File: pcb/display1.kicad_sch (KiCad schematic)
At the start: 35 parts, among them Q1 2N7002K, Q10 BSS84, Q11 BSS84, Q12 BSS84, Q2 2N7002K, Q3 2N7002K, Q4 2N7002K, Q5 BSS84, Q6 BSS84, Q7 BSS84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

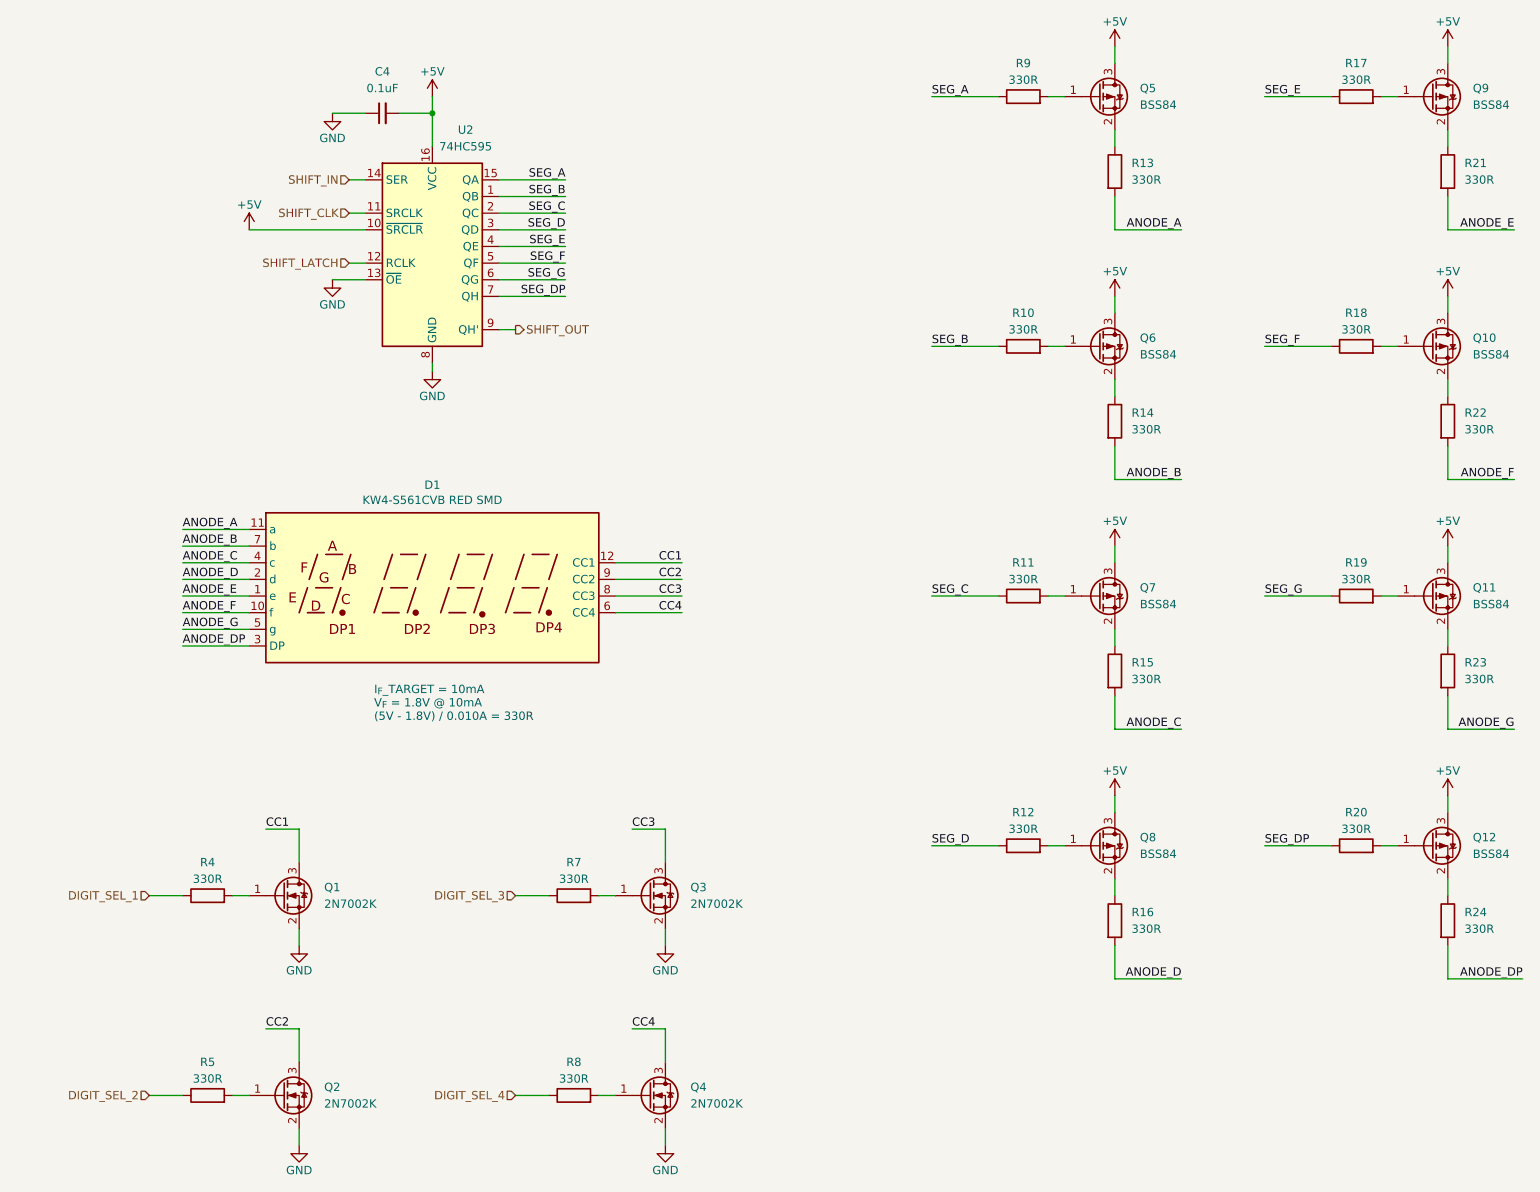
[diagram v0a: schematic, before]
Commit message: tentative schematic for common cathode
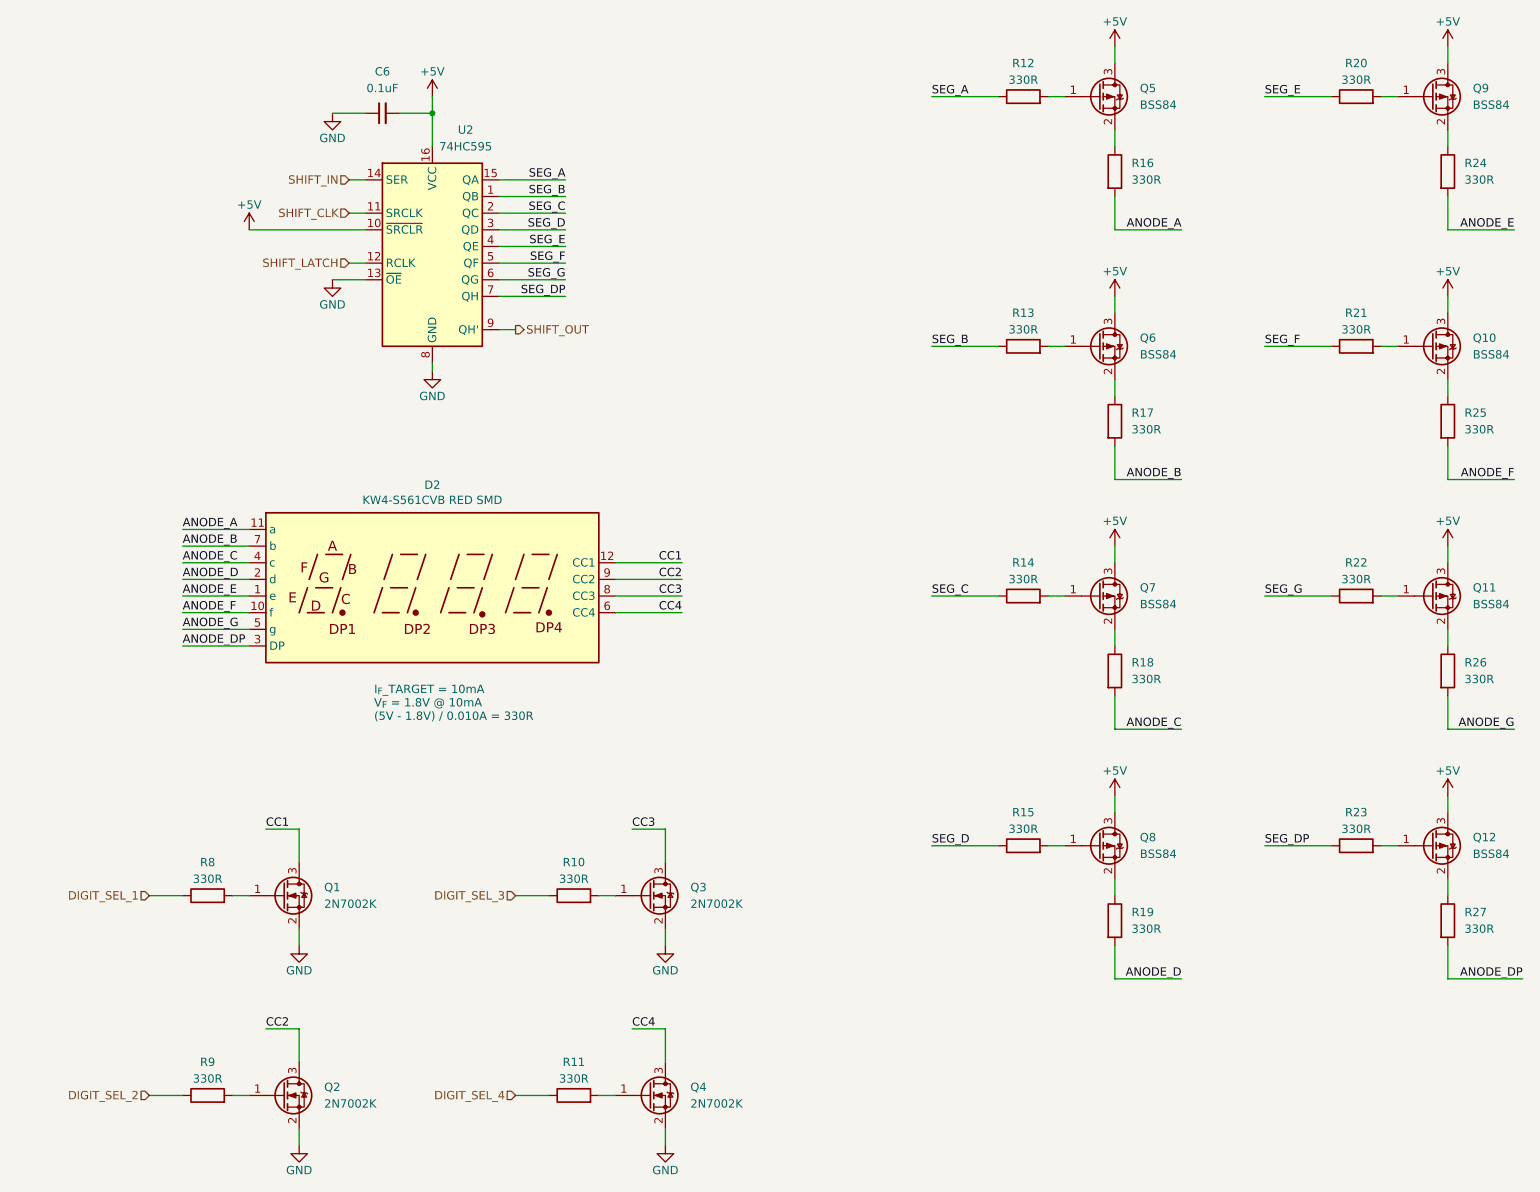
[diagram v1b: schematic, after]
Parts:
- C6: renamed from C4; footprint (none) -> Capacitor_SMD:C_0805_2012Metric_Pad1.18x1.45mm_HandSolder
- R10: renamed from R7; footprint Resistor_SMD:R_0805_2012Metric_Pad1.15x1.40mm_HandSolder -> Resistor_SMD:R_0805_2012Metric_Pad1.20x1.40mm_HandSolder
- R11: renamed from R8; footprint Resistor_SMD:R_0805_2012Metric_Pad1.15x1.40mm_HandSolder -> Resistor_SMD:R_0805_2012Metric_Pad1.20x1.40mm_HandSolder
- R12: renamed from R9; footprint Resistor_SMD:R_0805_2012Metric_Pad1.15x1.40mm_HandSolder -> Resistor_SMD:R_0805_2012Metric_Pad1.20x1.40mm_HandSolder
- R13: renamed from R10; footprint Resistor_SMD:R_0805_2012Metric_Pad1.15x1.40mm_HandSolder -> Resistor_SMD:R_0805_2012Metric_Pad1.20x1.40mm_HandSolder
- R14: renamed from R11; footprint Resistor_SMD:R_0805_2012Metric_Pad1.15x1.40mm_HandSolder -> Resistor_SMD:R_0805_2012Metric_Pad1.20x1.40mm_HandSolder
- R15: renamed from R12; footprint Resistor_SMD:R_0805_2012Metric_Pad1.15x1.40mm_HandSolder -> Resistor_SMD:R_0805_2012Metric_Pad1.20x1.40mm_HandSolder
- R16: renamed from R13; footprint (none) -> Resistor_SMD:R_0805_2012Metric_Pad1.20x1.40mm_HandSolder
- R17: renamed from R14; footprint (none) -> Resistor_SMD:R_0805_2012Metric_Pad1.20x1.40mm_HandSolder
- R18: renamed from R15; footprint (none) -> Resistor_SMD:R_0805_2012Metric_Pad1.20x1.40mm_HandSolder
- R19: renamed from R16; footprint (none) -> Resistor_SMD:R_0805_2012Metric_Pad1.20x1.40mm_HandSolder
- R20: renamed from R17; footprint Resistor_SMD:R_0805_2012Metric_Pad1.15x1.40mm_HandSolder -> Resistor_SMD:R_0805_2012Metric_Pad1.20x1.40mm_HandSolder
- R21: renamed from R18; footprint Resistor_SMD:R_0805_2012Metric_Pad1.15x1.40mm_HandSolder -> Resistor_SMD:R_0805_2012Metric_Pad1.20x1.40mm_HandSolder
- R22: renamed from R19; footprint Resistor_SMD:R_0805_2012Metric_Pad1.15x1.40mm_HandSolder -> Resistor_SMD:R_0805_2012Metric_Pad1.20x1.40mm_HandSolder
- R23: renamed from R20; footprint Resistor_SMD:R_0805_2012Metric_Pad1.15x1.40mm_HandSolder -> Resistor_SMD:R_0805_2012Metric_Pad1.20x1.40mm_HandSolder
- R24: renamed from R21; footprint (none) -> Resistor_SMD:R_0805_2012Metric_Pad1.20x1.40mm_HandSolder
- R25: renamed from R22; footprint (none) -> Resistor_SMD:R_0805_2012Metric_Pad1.20x1.40mm_HandSolder
- R26: renamed from R23; footprint (none) -> Resistor_SMD:R_0805_2012Metric_Pad1.20x1.40mm_HandSolder
- R27: renamed from R24; footprint (none) -> Resistor_SMD:R_0805_2012Metric_Pad1.20x1.40mm_HandSolder
- R8: renamed from R4; footprint Resistor_SMD:R_0805_2012Metric_Pad1.15x1.40mm_HandSolder -> Resistor_SMD:R_0805_2012Metric_Pad1.20x1.40mm_HandSolder
- R9: renamed from R5; footprint Resistor_SMD:R_0805_2012Metric_Pad1.15x1.40mm_HandSolder -> Resistor_SMD:R_0805_2012Metric_Pad1.20x1.40mm_HandSolder
- renumbered D1 to D2

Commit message: common anode schematic
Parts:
- removed C6: 0.1uF, Capacitor_SMD:C_0805_2012Metric_Pad1.18x1.45mm_HandSolder, symbol Device:C_Small
- removed D2: KW4-S561CVB RED SMD, mtg_life_counter:KW4-S561xxB_SMD, symbol mtg_life_counter:KW4-S561CxB
- removed Q1, Q2, Q3, Q4: 2N7002K, Package_TO_SOT_SMD:SOT-23, symbol Transistor_FET:2N7002K
- removed Q10, Q11, Q12, Q5, Q6, Q7, Q8, Q9: BSS84, Package_TO_SOT_SMD:SOT-23, symbol Transistor_FET:BSS84
- removed R21, R22, R23, R24, R25, R26, R27: 330R, Resistor_SMD:R_0805_2012Metric_Pad1.20x1.40mm_HandSolder, symbol Device:R
- removed U2: 74HC595, Package_SO:SOIC-16_3.9x9.9mm_P1.27mm, symbol 74xx:74HC595
- added D2: KW4-S561AVB, mtg_life_counter:KW4-S561xxB_SMD, symbol mtg_life_counter:KW4-S561AxB
- added Q1, Q2, Q3, Q4: DMG2301L, Package_TO_SOT_SMD:SOT-23, symbol Transistor_FET:DMG2301L
- added U2: TPIC6C596, Package_SO:SOIC-16_3.9x9.9mm_P1.27mm, symbol mtg_life_counter:TPIC6C596
- R20: value 330R -> 10k
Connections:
- net SEG_E is gone; now on net +5V: R20.1
- net +5V: now also Q1.3 (D), Q2.3 (D), Q3.3 (D), Q4.3 (D), U2.1 (VCC)
- net GND: now also U2.16 (GND), U2.8 (~{G})
- net SHIFT_CLK: now also U2.15 (SRCK)
- net SHIFT_IN: now also U2.2 (SER_IN)
- net SHIFT_LATCH: now also U2.10 (RCLK)
- net SHIFT_OUT: now also U2.9 (SER_OUT)
- net at R10.2: now also Q3.1 (G)
- net at R9.2: now also Q2.1 (G)
- net SD: now reaches R15.2
- net SD: now also U2.6 (DRAIN3)
- net at R11.2: now also Q4.1 (G)
- net SC: now reaches R14.2
- net SC: now also U2.5 (DRAIN2)
- net ADP: now reaches R19.1
- net ADP: now also D2.3 (DP)
- net SB: now reaches R13.2
- net SB: now also U2.4 (DRAIN1)
- net AF: now reaches R17.1
- net AF: now also D2.10 (f)
- net at R8.2: now also Q1.1 (G)
- net AG: now reaches R18.1
- net AG: now also D2.5 (g)
- net AE: now reaches R16.1
- net AE: now also D2.1 (e)
- net at R20.2: now also U2.7 (~{SRCLR})
- net SA: now reaches R12.2
- net SA: now also U2.3 (DRAIN0)
- net ANODE_A renamed SE
- net SE: now also U2.11 (DRAIN4)
- net ANODE_B renamed SF
- net SF: now also U2.12 (DRAIN5)
- net ANODE_C renamed SG
- net SG: now also U2.13 (DRAIN6)
- net ANODE_D renamed SDP
- net SDP: now also U2.14 (DRAIN7)
- net SEG_A renamed AA
- net AA: now also D2.11 (a)
- net SEG_B renamed AB
- net AB: now also D2.7 (b)
- net SEG_C renamed AC
- net AC: now also D2.4 (c)
- net SEG_D renamed AD
- net AD: now also D2.2 (d)
- new net CA1: D2.12 (CA1), Q1.2 (S)
- new net CA2: D2.9 (CA2), Q2.2 (S)
- new net CA3: D2.8 (CA3), Q3.2 (S)
- new net CA4: D2.6 (CA4), Q4.2 (S)

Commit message: continue wip
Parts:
- added C7: 0.1uF, Capacitor_SMD:C_0805_2012Metric_Pad1.18x1.45mm_HandSolder, symbol Device:C_Small
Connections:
- net +5V: now also C7.1
- net GND: now also C7.2
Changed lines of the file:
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@@
+	(wire
+		(pts
+			(xy 200.66 58.42) (xy 200.66 60.96)
+		)
+		(stroke
+			(width 0)
+			(type default)
+		)
+	)
 	(wire
 		(pts
@@
 		(pts
 			(xy 223.52 86.36) (xy 228.6 86.36)
+		)
+		(stroke
+			(width 0)
+			(type default)
+		)
+	)
+	(wire
+		(pts
+			(xy 200.66 50.8) (xy 200.66 53.34)
 		)
 		(stroke
@@
 	)
 	(symbol
+		(lib_id "power:GND")
+		(at 200.66 60.96 0)
+		(unit 1)
+		(exclude_from_sim no)
+		(in_bom yes)
+		(on_board yes)
+		(dnp no)
+		(property "Reference" "#PWR066"
+			(at 200.66 67.31 0)
+			(effects
+				(font
+					(size 1.27 1.27)
+				)
+				(hide yes)
+			)
+		)
+		(property "Value" "GND"
+			(at 200.66 64.77 0)
+			(effects
+				(font
+					(size 1.27 1.27)
+				)
+			)
+		)
+		(property "Footprint" ""
+			(at 200.66 60.96 0)
+			(effects
+				(font
+					(size 1.27 1.27)
+				)
+				(hide yes)
+			)
+		)
+		(property "Datasheet" ""
+			(at 200.66 60.96 0)
+			(effects
+				(font
+					(size 1.27 1.27)
+				)
+				(hide yes)
+			)
+		)
+		(property "Description" "Power symbol creates a global label with name \"GND\" , ground"
+			(at 200.66 60.96 0)
+			(effects
+				(font
+					(size 1.27 1.27)
+				)
+				(hide yes)
+			)
+		)
+		(pin "1"
+		)
+		(instances
+			(project "mtg_life_counter"
+				(path "/1883df74-0bd5-446c-9076-f848bb3cfebf/783ca70e-2b43-402c-8078-60ba3aaea8cd"
+					(reference "#PWR066")
+					(unit 1)
+				)
+			)
+		)
+	)
+	(symbol
 		(lib_id "Device:R")
 		(at 49.53 63.5 90)
@@
 	)
 	(symbol
+		(lib_id "Device:C_Small")
+		(at 200.66 55.88 0)
+		(mirror y)
+		(unit 1)
+		(exclude_from_sim no)
+		(in_bom yes)
+		(on_board yes)
+		(dnp no)
+		(fields_autoplaced yes)
+		(property "Reference" "C7"
+			(at 203.2 54.6162 0)
+			(effects
+				(font
+					(size 1.27 1.27)
+				)
+				(justify right)
+			)
+		)
+		(property "Value" "0.1uF"
+			(at 203.2 57.1562 0)
+			(effects
+				(font
+					(size 1.27 1.27)
+				)
+				(justify right)
+			)
+		)
+		(property "Footprint" "Capacitor_SMD:C_0805_2012Metric_Pad1.18x1.45mm_HandSolder"
+			(at 200.66 55.88 0)
+			(effects
+				(font
+					(size 1.27 1.27)
+				)
+				(hide yes)
+			)
+		)
+		(property "Datasheet" "~"
+			(at 200.66 55.88 0)
+			(effects
+				(font
+					(size 1.27 1.27)
+				)
+				(hide yes)
+			)
+		)
+		(property "Description" "Unpolarized capacitor, small symbol"
+			(at 200.66 55.88 0)
+			(effects
+				(font
+					(size 1.27 1.27)
+				)
+				(hide yes)
+			)
+		)
+		(pin "2"
+		)
+		(pin "1"
+		)
+		(instances
+			(project "mtg_life_counter"
+				(path "/1883df74-0bd5-446c-9076-f848bb3cfebf/783ca70e-2b43-402c-8078-60ba3aaea8cd"
+					(reference "C7")
+					(unit 1)
+				)
+			)
+		)
+	)
+	(symbol
 		(lib_id "Device:R")
 		(at 49.53 33.02 90)
@@
 					(unit 1)
 				)
+			)
+		)
+	)
+	(symbol
+		(lib_id "power:+5V")
+		(at 200.66 50.8 0)
+		(unit 1)
+		(exclude_from_sim no)
+		(in_bom yes)
+		(on_board yes)
+		(dnp no)
+		(property "Reference" "#PWR065"
+			(at 200.66 54.61 0)
+			(effects
+				(font
+					(size 1.27 1.27)
+				)
+				(hide yes)
+			)
+		)
+		(property "Value" "+5V"
+			(at 200.66 46.99 0)
+			(effects
+				(font
+					(size 1.27 1.27)
+				)
+			)
+		)
+		(property "Footprint" ""
+			(at 200.66 50.8 0)
+			(effects
+				(font
+					(size 1.27 1.27)
+				)
+				(hide yes)
+			)
+		)
+		(property "Datasheet" ""
+			(at 200.66 50.8 0)
+			(effects
+				(font
+					(size 1.27 1.27)
+				)
+				(hide yes)
+			)
+		)
+		(property "Description" "Power symbol creates a global label with name \"+5V\""
+			(at 200.66 50.8 0)
+			(effects
+				(font
+					(size 1.27 1.27)
+				)
+				(hide yes)
+			)
+		)
+		(pin "1"
+		)
+		(instances
+			(project "mtg_life_counter"
+				(path "/1883df74-0bd5-446c-9076-f848bb3cfebf/783ca70e-2b43-402c-8078-60ba3aaea8cd"
+					(reference "#PWR065")
+					(unit 1)
+				)
